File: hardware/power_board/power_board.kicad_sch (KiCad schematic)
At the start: 2 parts, among them J1 MCU, J9 MAINS_IN

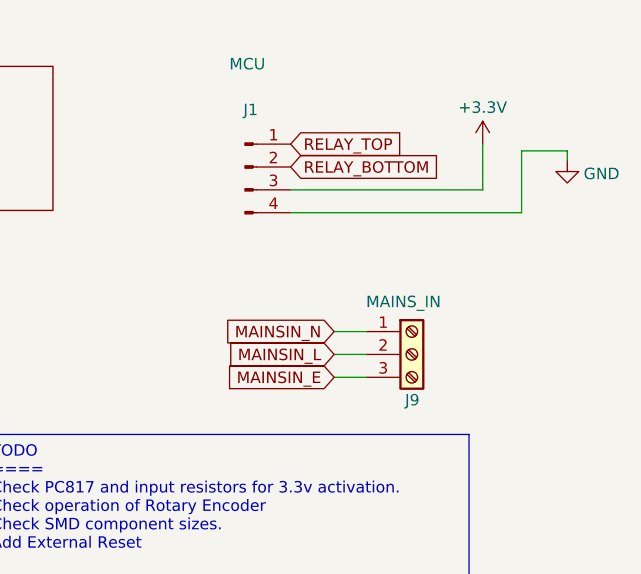
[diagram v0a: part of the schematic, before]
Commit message: v2 Power/Relay PCB
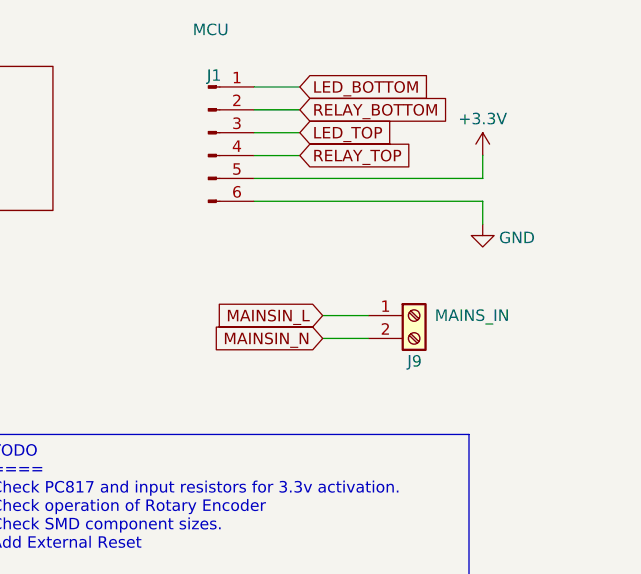
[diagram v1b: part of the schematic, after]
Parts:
- J1: footprint Connector_PinHeader_2.54mm:PinHeader_1x04_P2.54mm_Vertical -> Connector_PinHeader_2.54mm:PinHeader_1x06_P2.54mm_Vertical; symbol Connector:Conn_01x04_Pin -> Connector:Conn_01x06_Pin
- J9: footprint TerminalBlock_Dinkle:TerminalBlock_Dinkle_DT-55-B01X-03_P10.00mm -> TerminalBlock_Dinkle:TerminalBlock_Dinkle_DT-55-B01X-02_P10.00mm; symbol Connector:Screw_Terminal_01x03 -> Connector:Screw_Terminal_01x02
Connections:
- net +3.3V: now also J1.5 (Pin_5); no longer J1.3 (Pin_3)
- net GND: now also J1.6 (Pin_6); no longer J1.4 (Pin_4)
- net MAINSIN_L: now also J9.1 (Pin_1); no longer J9.2 (Pin_2)
- net MAINSIN_N: now also J9.2 (Pin_2); no longer J9.1 (Pin_1)
- net RELAY_TOP: now also J1.4 (Pin_4); no longer J1.1 (Pin_1)
- removed net MAINSIN_E: J9.3 (Pin_3)
- new net LED_BOTTOM: J1.1 (Pin_1)
- new net LED_TOP: J1.3 (Pin_3)

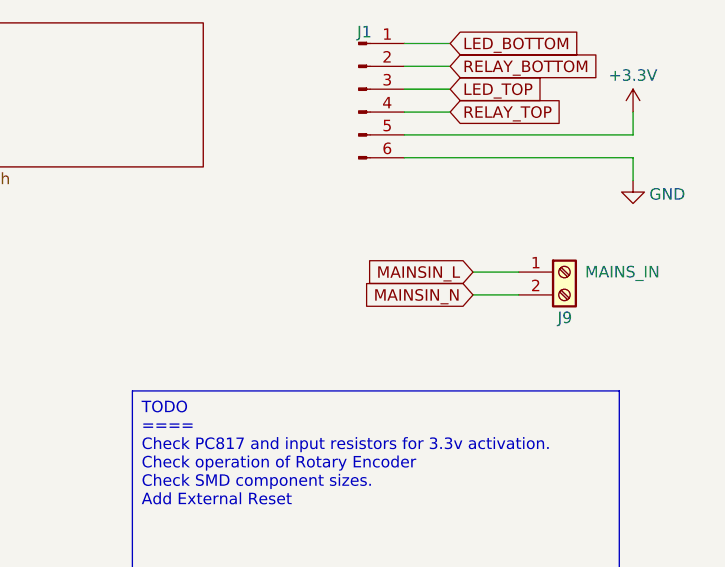
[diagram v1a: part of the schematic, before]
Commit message: Refactored PCBs for v2. See README
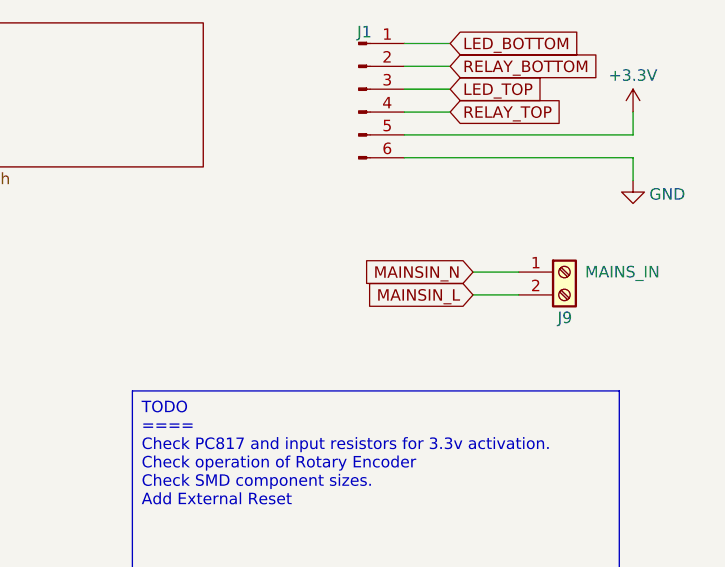
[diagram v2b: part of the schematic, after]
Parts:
- J9: footprint TerminalBlock_Dinkle:TerminalBlock_Dinkle_DT-55-B01X-02_P10.00mm -> TerminalBlock2:HB9500-9.5-2P
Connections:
- net MAINSIN_L: now also J9.2 (Pin_2); no longer J9.1 (Pin_1)
- net MAINSIN_N: now also J9.1 (Pin_1); no longer J9.2 (Pin_2)
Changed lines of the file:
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@@
-    (stroke (width 0) (type default))
-  )
-  (wire (pts (xy 165.1 71.12) (xy 170.18 71.12))
     (stroke (width 0) (type default))
   )
@@
   )
   (wire (pts (xy 182.88 50.8) (xy 182.88 53.34))
+    (stroke (width 0) (type default))
+  )
+  (wire (pts (xy 165.1 71.12) (xy 170.18 71.12))
     (stroke (width 0) (type default))
   )
@@
     )
   )
-  (global_label "MAINSIN_L" (shape input) (at 165.1 68.58 180) (fields_autoplaced)
+  (global_label "MAINSIN_L" (shape input) (at 165.1 71.12 180) (fields_autoplaced)
     (effects (font (size 1.27 1.27)) (justify right))
-    (property "Intersheetrefs" "${INTERSHEET_REFS}" (at 152.5784 68.58 0)
+    (property "Intersheetrefs" "${INTERSHEET_REFS}" (at 152.5784 71.12 0)
       (effects (font (size 1.27 1.27)) (justify right) hide)
     )
@@
     )
   )
-  (global_label "MAINSIN_N" (shape input) (at 165.1 71.12 180) (fields_autoplaced)
+  (global_label "MAINSIN_N" (shape input) (at 165.1 68.58 180) (fields_autoplaced)
     (effects (font (size 1.27 1.27)) (justify right))
-    (property "Intersheetrefs" "${INTERSHEET_REFS}" (at 152.276 71.12 0)
+    (property "Intersheetrefs" "${INTERSHEET_REFS}" (at 152.276 68.58 0)
       (effects (font (size 1.27 1.27)) (justify right) hide)
     )
@@
       (effects (font (size 1.27 1.27)) (justify left))
     )
-    (property "Footprint" "TerminalBlock_Dinkle:TerminalBlock_Dinkle_DT-55-B01X-02_P10.00mm" (at 175.26 68.58 0)
+    (property "Footprint" "TerminalBlock2:HB9500-9.5-2P" (at 175.26 68.58 0)
       (effects (font (size 1.27 1.27)) hide)
     )

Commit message: v2 Boards for fabrication
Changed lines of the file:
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@@
     )
   )
-  (global_label "LED_BOTTOM" (shape input) (at 162.56 43.18 0) (fields_autoplaced)
+  (global_label "LED_BOTTOM" (shape output) (at 162.56 43.18 0) (fields_autoplaced)
     (effects (font (size 1.27 1.27)) (justify left))
     (property "Intersheetrefs" "${INTERSHEET_REFS}" (at 177.2775 43.18 0)
@@
     )
   )
-  (global_label "LED_TOP" (shape input) (at 162.56 48.26 0) (fields_autoplaced)
+  (global_label "LED_TOP" (shape output) (at 162.56 48.26 0) (fields_autoplaced)
     (effects (font (size 1.27 1.27)) (justify left))
     (property "Intersheetrefs" "${INTERSHEET_REFS}" (at 173.528 48.26 0)

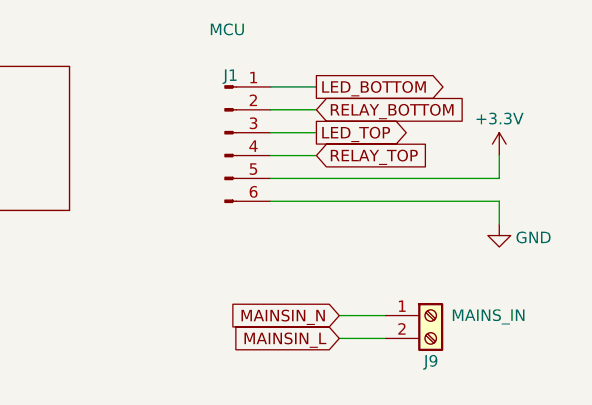
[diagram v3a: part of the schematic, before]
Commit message: Add missing holes and fabrication marks
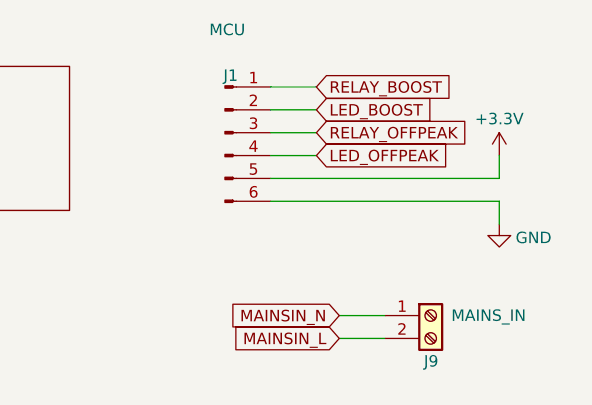
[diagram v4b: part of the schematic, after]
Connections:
- net LED_BOTTOM renamed RELAY_BOOST
- net LED_TOP renamed RELAY_OFFPEAK
- net RELAY_BOTTOM renamed LED_BOOST
- net RELAY_TOP renamed LED_OFFPEAK
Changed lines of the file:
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@@
 (kicad_sch (version 20230121) (generator eeschema)
   (paper "A4")
-  (wire (pts (xy 157.48 43.18) (xy 162.56 43.18))
-    (stroke (width 0) (type default))
-  )
-  (wire (pts (xy 165.1 68.58) (xy 170.18 68.58))
+  (wire (pts (xy 157.48 48.26) (xy 162.56 48.26))
     (stroke (width 0) (type default))
   )
@@
     (stroke (width 0) (type default))
   )
-  (wire (pts (xy 157.48 48.26) (xy 162.56 48.26))
-    (stroke (width 0) (type default))
-  )
-  (wire (pts (xy 157.48 45.72) (xy 162.56 45.72))
+  (wire (pts (xy 165.1 68.58) (xy 170.18 68.58))
     (stroke (width 0) (type default))
   )
@@
     (stroke (width 0) (type default))
   )
+  (wire (pts (xy 157.48 43.18) (xy 162.56 43.18))
+    (stroke (width 0) (type default))
+  )
+  (wire (pts (xy 157.48 45.72) (xy 162.56 45.72))
+    (stroke (width 0) (type default))
+  )
   (text_box "or UL or IEC testing, all the components must be certified, if the components are not certified then you'll foot the bill for the testing. So the first step would be to establish where you want to sell the product, then find the regulatory standards that you need for the product."
     (at 57.658 80.772 0) (size 46.228 23.114)
@@
     (effects (font (size 1.27 1.27)) (justify left top))
   )
-  (global_label "RELAY_BOTTOM" (shape input) (at 162.56 45.72 0) (fields_autoplaced)
+  (global_label "RELAY_OFFPEAK" (shape input) (at 162.56 48.26 0) (fields_autoplaced)
     (effects (font (size 1.27 1.27)) (justify left))
-    (property "Intersheetrefs" "${INTERSHEET_REFS}" (at 179.4547 45.72 0)
+    (property "Intersheetrefs" "${INTERSHEET_REFS}" (at 180.4224 48.26 0)
       (effects (font (size 1.27 1.27)) (justify left) hide)
     )
   )
-  (global_label "LED_BOTTOM" (shape output) (at 162.56 43.18 0) (fields_autoplaced)
+  (global_label "LED_OFFPEAK" (shape input) (at 162.56 50.8 0) (fields_autoplaced)
     (effects (font (size 1.27 1.27)) (justify left))
-    (property "Intersheetrefs" "${INTERSHEET_REFS}" (at 177.2775 43.18 0)
+    (property "Intersheetrefs" "${INTERSHEET_REFS}" (at 178.2452 50.8 0)
       (effects (font (size 1.27 1.27)) (justify left) hide)
     )
   )
-  (global_label "LED_TOP" (shape output) (at 162.56 48.26 0) (fields_autoplaced)
+  (global_label "LED_BOOST" (shape input) (at 162.56 45.72 0) (fields_autoplaced)
     (effects (font (size 1.27 1.27)) (justify left))
-    (property "Intersheetrefs" "${INTERSHEET_REFS}" (at 173.528 48.26 0)
+    (property "Intersheetrefs" "${INTERSHEET_REFS}" (at 176.068 45.72 0)
       (effects (font (size 1.27 1.27)) (justify left) hide)
     )
@@
     )
   )
-  (global_label "RELAY_TOP" (shape input) (at 162.56 50.8 0) (fields_autoplaced)
+  (global_label "RELAY_BOOST" (shape input) (at 162.56 43.18 0) (fields_autoplaced)
     (effects (font (size 1.27 1.27)) (justify left))
-    (property "Intersheetrefs" "${INTERSHEET_REFS}" (at 175.7052 50.8 0)
+    (property "Intersheetrefs" "${INTERSHEET_REFS}" (at 178.2452 43.18 0)
       (effects (font (size 1.27 1.27)) (justify left) hide)
     )

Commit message: fix boards so they components are on the correct side lol
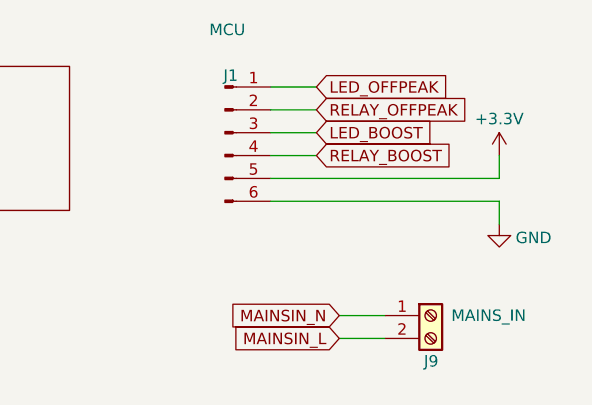
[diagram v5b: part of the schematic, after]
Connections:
- net LED_BOOST: now also J1.3 (Pin_3); no longer J1.2 (Pin_2)
- net LED_OFFPEAK: now also J1.1 (Pin_1); no longer J1.4 (Pin_4)
- net RELAY_BOOST: now also J1.4 (Pin_4); no longer J1.1 (Pin_1)
- net RELAY_OFFPEAK: now also J1.2 (Pin_2); no longer J1.3 (Pin_3)
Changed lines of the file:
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@@
 (kicad_sch (version 20230121) (generator eeschema)
   (paper "A4")
+  (wire (pts (xy 157.48 45.72) (xy 162.56 45.72))
+    (stroke (width 0) (type default))
+  )
   (wire (pts (xy 157.48 48.26) (xy 162.56 48.26))
     (stroke (width 0) (type default))
@@
     (stroke (width 0) (type default))
   )
-  (wire (pts (xy 157.48 45.72) (xy 162.56 45.72))
-    (stroke (width 0) (type default))
-  )
   (text_box "or UL or IEC testing, all the components must be certified, if the components are not certified then you'll foot the bill for the testing. So the first step would be to establish where you want to sell the product, then find the regulatory standards that you need for the product."
     (at 57.658 80.772 0) (size 46.228 23.114)
@@
     (effects (font (size 1.27 1.27)) (justify left top))
   )
-  (global_label "RELAY_OFFPEAK" (shape input) (at 162.56 48.26 0) (fields_autoplaced)
+  (global_label "RELAY_OFFPEAK" (shape input) (at 162.56 45.72 0) (fields_autoplaced)
     (effects (font (size 1.27 1.27)) (justify left))
-    (property "Intersheetrefs" "${INTERSHEET_REFS}" (at 180.4224 48.26 0)
+    (property "Intersheetrefs" "${INTERSHEET_REFS}" (at 180.4224 45.72 0)
       (effects (font (size 1.27 1.27)) (justify left) hide)
     )
   )
-  (global_label "LED_OFFPEAK" (shape input) (at 162.56 50.8 0) (fields_autoplaced)
+  (global_label "LED_OFFPEAK" (shape input) (at 162.56 43.18 0) (fields_autoplaced)
     (effects (font (size 1.27 1.27)) (justify left))
-    (property "Intersheetrefs" "${INTERSHEET_REFS}" (at 178.2452 50.8 0)
+    (property "Intersheetrefs" "${INTERSHEET_REFS}" (at 178.2452 43.18 0)
       (effects (font (size 1.27 1.27)) (justify left) hide)
     )
   )
-  (global_label "LED_BOOST" (shape input) (at 162.56 45.72 0) (fields_autoplaced)
+  (global_label "LED_BOOST" (shape input) (at 162.56 48.26 0) (fields_autoplaced)
     (effects (font (size 1.27 1.27)) (justify left))
-    (property "Intersheetrefs" "${INTERSHEET_REFS}" (at 176.068 45.72 0)
+    (property "Intersheetrefs" "${INTERSHEET_REFS}" (at 176.068 48.26 0)
       (effects (font (size 1.27 1.27)) (justify left) hide)
     )
@@
     )
   )
-  (global_label "RELAY_BOOST" (shape input) (at 162.56 43.18 0) (fields_autoplaced)
+  (global_label "RELAY_BOOST" (shape input) (at 162.56 50.8 0) (fields_autoplaced)
     (effects (font (size 1.27 1.27)) (justify left))
-    (property "Intersheetrefs" "${INTERSHEET_REFS}" (at 178.2452 43.18 0)
+    (property "Intersheetrefs" "${INTERSHEET_REFS}" (at 178.2452 50.8 0)
       (effects (font (size 1.27 1.27)) (justify left) hide)
     )
